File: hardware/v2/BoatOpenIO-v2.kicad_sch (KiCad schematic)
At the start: 48 parts, among them J1 Conn_01x03_Pin, J10 Conn_01x03_Pin, J11 Conn_01x03_Pin, J12 Conn_01x03_Pin, J13 Conn_01x03_Pin, J14 Conn_01x03_Pin, J15 Conn_01x03_Pin, J16 Conn_01x03_Pin, J17 Conn_01x02, J18 Conn_01x02, J19 Conn_01x02, J2 Conn_01x03_Pin, J20 Conn_01x02, J21 Conn_01x02, J22 Conn_01x02, J23 Conn_01x02, J24 Conn_01x02, J25 Conn_01x02, J26 Conn_01x02, J27 Screw_Terminal_01x16, J28 Conn_01x02, J29 Conn_02x10_Odd_Even, J3 Conn_01x03_Pin, J30 Conn_02x10_Odd_Even, J31 Conn_01x03_Pin, J32 Conn_01x03_Pin, J33 Conn_02x08_Odd_Even, J34 Conn_02x08_Odd_Even, J35 Conn_02x05_Odd_Even, J4 Conn_01x03_Pin, J5 Conn_01x03_Pin, J6 Conn_01x03_Pin, J7 Conn_01x03_Pin, J8 Conn_01x03_Pin, J9 Conn_01x03_Pin, U1 ESP32-WROOM-32D, U2 MPU6050, U3 ZC261500, U7 BOB-09056, U8 AMS1117CD-3.3

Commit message: Hardware v2: Schaltplan aktualisiert, Netzliste + PNG-Export, Prototyp-Bilder nach v1_proto/
- KiCad-Schaltplaene aktualisiert (Mainboard, ESP32-Adapter, Eingangsboard, VCC)
- Netzliste BoatOpenIO-v2.net exportiert
- Schaltplan-Uebersicht als images/schaltplan_v2.png
- v1-Prototyp-Fotos nach images/v1_proto/ verschoben

Co-Authored-By: Claude Opus 4.8 <noreply@anthropic.com>
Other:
- title: (none) -> BoatOpenIO
- moved on the sheet: D1, D2, D3, D4, D5, D6, J1, J10, J11, J12, J13, J14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

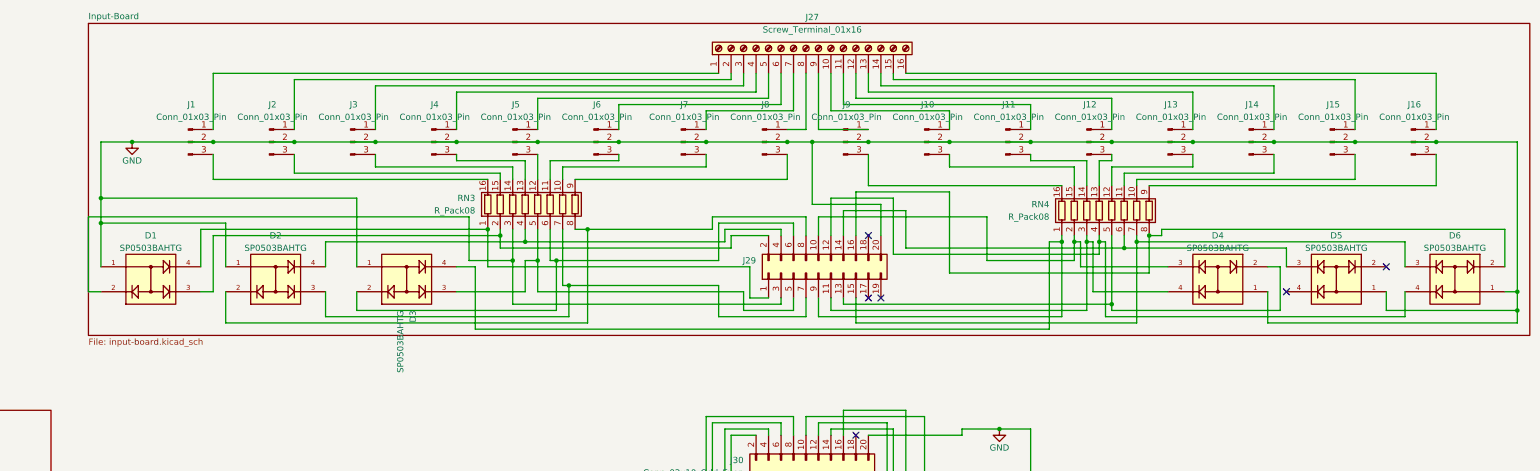
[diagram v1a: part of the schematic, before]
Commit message: Hardware v2: Input-Board neu generiert (Rev.1/Rev.2)
Gerber neu erzeugt, rev1/rev2-ZIP und Pick-&-Place-CSV ergänzt,
Schaltplan/Layout und Projektdateien aktualisiert.

Co-Authored-By: Claude Opus 4.8 <noreply@anthropic.com>
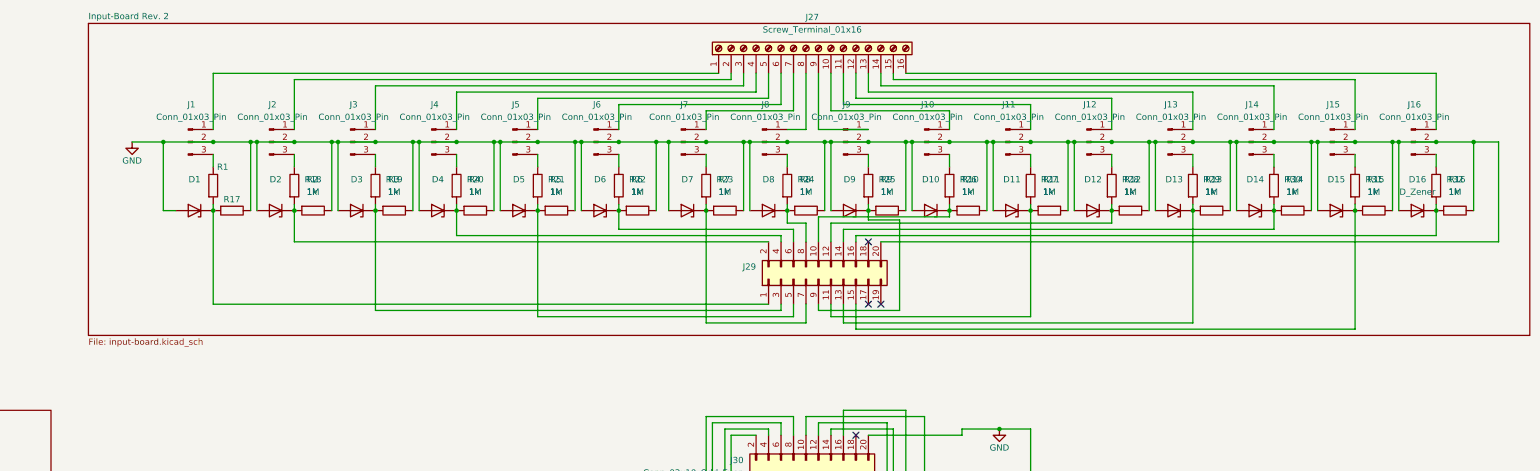
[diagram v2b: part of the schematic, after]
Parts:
- removed D1, D2, D3, D4, D5, D6: SP0503BAHTG, Package_TO_SOT_SMD:SOT-143_Handsoldering, symbol SP0503BAHTG:SP0503BAHTG
- removed RN3, RN4: R_Pack08, PCM_SparkFun-Semiconductor-Standard:DIP-16, symbol Device:R_Pack08
- added D1, D10, D11, D12, D13, D14, D15, D16, D2, D3, D4, D5, D6, D7, D8, D9: D_Zener, PCM_Diode_SMD_AKL:D_SOD-123_Zener, symbol Device:D_Zener
- added R1, R10, R11, R12, R13, R14, R15, R16, R2, R3, R4, R5, R6, R7, R8, R9: 1k, Resistor_SMD:R_0805_2012Metric, symbol PCM_SL_Resistors:1k
- added R17, R18, R19, R20, R21, R22, R23, R24, R25, R26, R27, R28, R29, R30, R31, R32: 1M, Resistor_SMD:R_0805_2012Metric, symbol PCM_SL_Resistors:1M
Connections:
- net GND: now also D1.2 (A), D10.2 (A), D11.2 (A), D12.2 (A), D13.2 (A), D14.2 (A), D15.2 (A), D16.2 (A), D2.2 (A), D3.2 (A), D4.2 (A), D5.2 (A), D6.2 (A), D7.2 (A), D8.2 (A), D9.2 (A), R17.2, R18.2, R19.2, R20.2, R21.2, R22.2, R23.2, R24.2, R25.2, R26.2, R27.2, R28.2, R29.2, R30.2, R31.2, R32.2
- net at J6.3 (Pin_3): now also R6.2
- net at J29.1 (Pin_1): now also D1.1 (K), R1.1, R17.1
- net at J29.10 (Pin_10): now also D10.1 (K), R10.1, R26.1
- net at J29.11 (Pin_11): now also D11.1 (K), R11.1, R27.1
- net at J29.12 (Pin_12): now also D12.1 (K), R12.1, R28.1
- net at J29.13 (Pin_13): now also D13.1 (K), R13.1, R29.1
- net at J29.14 (Pin_14): now also D14.1 (K), R14.1, R30.1
- net at J29.15 (Pin_15): now also D15.1 (K), R15.1, R31.1
- net at J29.16 (Pin_16): now also D16.1 (K), R16.1, R32.1
- net at J29.2 (Pin_2): now also D2.1 (K), R18.1, R2.1
- net at J29.3 (Pin_3): now also D3.1 (K), R19.1, R3.1
- net at J29.4 (Pin_4): now also D4.1 (K), R20.1, R4.1
- net at J29.5 (Pin_5): now also D5.1 (K), R21.1, R5.1
- net at J29.6 (Pin_6): now also D6.1 (K), R22.1, R6.1
- net at J29.7 (Pin_7): now also D7.1 (K), R23.1, R7.1
- net at J29.8 (Pin_8): now also D8.1 (K), R24.1, R8.1
- net at J29.9 (Pin_9): now also D9.1 (K), R25.1, R9.1
- net at J8.3 (Pin_3): now also R8.2
- net at J7.3 (Pin_3): now also R7.2
- net at J5.3 (Pin_3): now also R5.2
- net at J4.3 (Pin_3): now also R4.2
- net at J3.3 (Pin_3): now also R3.2
- net at J2.3 (Pin_3): now also R2.2
- net at J1.3 (Pin_3): now also R1.2
- net at J15.3 (Pin_3): now also R15.2
- net at J10.3 (Pin_3): now also R10.2
- net at J11.3 (Pin_3): now also R11.2
- net at J9.3 (Pin_3): now also R9.2
- net at J14.3 (Pin_3): now also R14.2
- net at J12.3 (Pin_3): now also R12.2
- net at J13.3 (Pin_3): now also R13.2
- net at J16.3 (Pin_3): now also R16.2
- no-connect marks 40 -> 38
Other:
- sheet Input-Board renamed Input-Board Rev. 2
- moved on the sheet: J29
